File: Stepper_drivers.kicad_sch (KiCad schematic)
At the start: 28 parts, among them J16 Conn_01x04_Socket, J17 Conn_01x02_Socket, J7 Conn_01x04_Socket, J8 Conn_01x02_Socket, U4 LTV-247, U6 AM26LS31CDR

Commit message: New PSU designs + footprints assigned. Changes to board shape to make room for new components. BOM consolidation of supplimentary file
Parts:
- J10: renamed from J8; Digikey Part Number 1818-QT04ADP83V0000G-ND -> 1818-QT02ADP83V0000G-ND; Digikey URL https://www.digikey.com.au/en/products/detail/amphenol-anytek/QT04ADP83V0000G/25618782 -> https://www.digikey.com.au/en/products/detail/amphenol-anytek/QT02ADP83V0000G/25618889
- J7: renamed from J16; Digikey Part Number 1818-QT02ADP83V0000G-ND -> 1818-QT04ADP83V0000G-ND; Digikey URL https://www.digikey.com.au/en/products/detail/amphenol-anytek/QT02ADP83V0000G/25618889 -> https://www.digikey.com.au/en/products/detail/amphenol-anytek/QT04ADP83V0000G/25618782
- J8: renamed from J17; Digikey Part Number 1818-QT04ADP83V0000G-ND -> 1818-QT02ADP83V0000G-ND; Digikey URL https://www.digikey.com.au/en/products/detail/amphenol-anytek/QT04ADP83V0000G/25618782 -> https://www.digikey.com.au/en/products/detail/amphenol-anytek/QT02ADP83V0000G/25618889
- J9: renamed from J7; Digikey Part Number 1818-QT02ADP83V0000G-ND -> 1818-QT04ADP83V0000G-ND; Digikey URL https://www.digikey.com.au/en/products/detail/amphenol-anytek/QT02ADP83V0000G/25618889 -> https://www.digikey.com.au/en/products/detail/amphenol-anytek/QT04ADP83V0000G/25618782
- renumbered C12 to C10, C16 to C11, C32 to C12, C20 to C13, C38 to C14, C11 to C9, R56 to R12, R59 to R13, R62 to R14, R65 to R15, R80 to R16, R83 to R17, R86 to R18, R89 to R19, R92 to R20, R104 to R21, R95 to R22, R105 to R23, R98 to R24, R106 to R25, R101 to R26, R107 to R27, U6 to U5

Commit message: Switched terminal footprints over to a finer pitch. Corrected an issue with component reference values preventing proper use of multi channel rule areas. Component references for 4 channel optos are more straightforward as a result
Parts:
- removed U4: LTV-247, Package_SO:SOP-16_4.4x10.4mm_P1.27mm, symbol Isolator:LTV-247
- added U (x4): LTV-247, Package_SO:SOP-16_4.4x10.4mm_P1.27mm, symbol Isolator:LTV-247
- J: renamed from J8; footprint Amphenol QT:QT02ADP83V0000G -> 691412120002B:691412120002B; Digikey Part Number 1818-QT02ADP83V0000G-ND -> 732-691412120002B-ND; Digikey URL https://www.digikey.com.au/en/products/detail/amphenol-anyt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 -> https://www.digikey.com.au/en/products/detail/w%C3%BCrth-el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
- J: renamed from J7; footprint Amphenol QT:QT04ADP83V0000G -> 691412120004B:691412120004B; Digikey Part Number 1818-QT04ADP83V0000G-ND -> 732-691412120004B-ND; Digikey URL https://www.digikey.com.au/en/products/detail/amphenol-anyt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 -> https://www.digikey.com.au/en/products/detail/w%C3%BCrth-el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
- J10: footprint Amphenol QT:QT02ADP83V0000G -> 691412120002B:691412120002B; Digikey Part Number 1818-QT02ADP83V0000G-ND -> 732-691412120002B-ND; Digikey URL https://www.digikey.com.au/en/products/detail/amphenol-anyt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 -> https://www.digikey.com.au/en/products/detail/w%C3%BCrth-el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
- J9: footprint Amphenol QT:QT04ADP83V0000G -> 691412120004B:691412120004B; Digikey Part Number 1818-QT04ADP83V0000G-ND -> 732-691412120004B-ND; Digikey URL https://www.digikey.com.au/en/products/detail/amphenol-anyt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 -> https://www.digikey.com.au/en/products/detail/w%C3%BCrth-el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
- renumbered U5 to U
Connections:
- net +5VD: now also U.16, U.16, U.16, U.16
- net GNDREF: now also U.2, U.2, U.2, U.2
- net at R12.2: now also U.1
- net at R17.2, U.7 (2A): now also U.15
- net at R13.2: now also U.1
- net at R19.2, U.15 (4A): now also U.15
- net at R16.2, U.1 (1A): now also U.15
- net at R18.2, U.9 (3A): now also U.15
- net at R14.2: now also U.1
- net at R15.2: now also U.1

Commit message: Added 3d Models for new terminal connectors for easy board verification before committing to build
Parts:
- renumbered J to J7, J to J8, U to U4, U to U5
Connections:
- net +5VD: now also U4.10, U4.12, U4.14; no longer U4.16, U4.16, U4.16
- net GNDREF: now also U4.4, U4.6, U4.8; no longer U4.2, U4.2, U4.2
- net at R15.2: now also U4.7; no longer U4.1
- net at R19.2, U5.15 (4A): now also U4.9; no longer U4.15
- net at R13.2: now also U4.3; no longer U4.1
- net at R17.2, U5.7 (2A): now also U4.13; no longer U4.15
- net at R18.2, U5.9 (3A): now also U4.11; no longer U4.15
- net at R14.2: now also U4.5; no longer U4.1

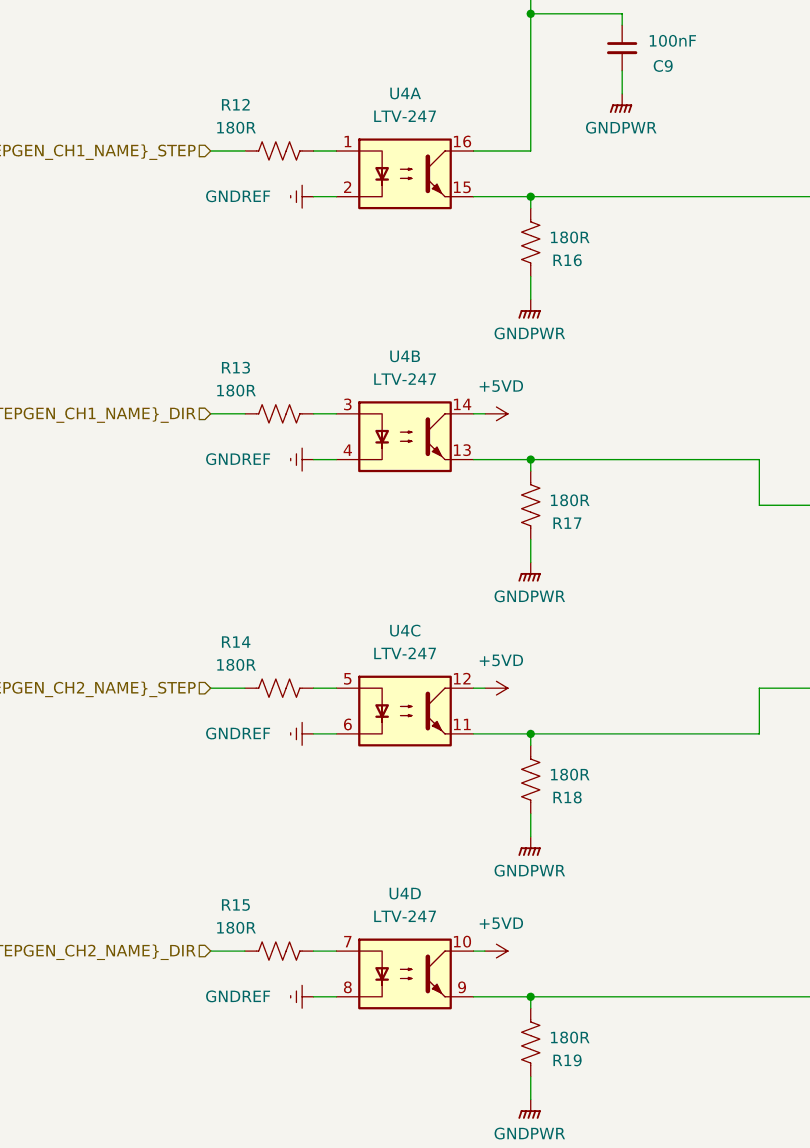
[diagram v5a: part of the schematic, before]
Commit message: Caught some errors with spacing of jumpers, did some BOM consolidation and included BOM. Updates to Gerbers to reflect new changes.
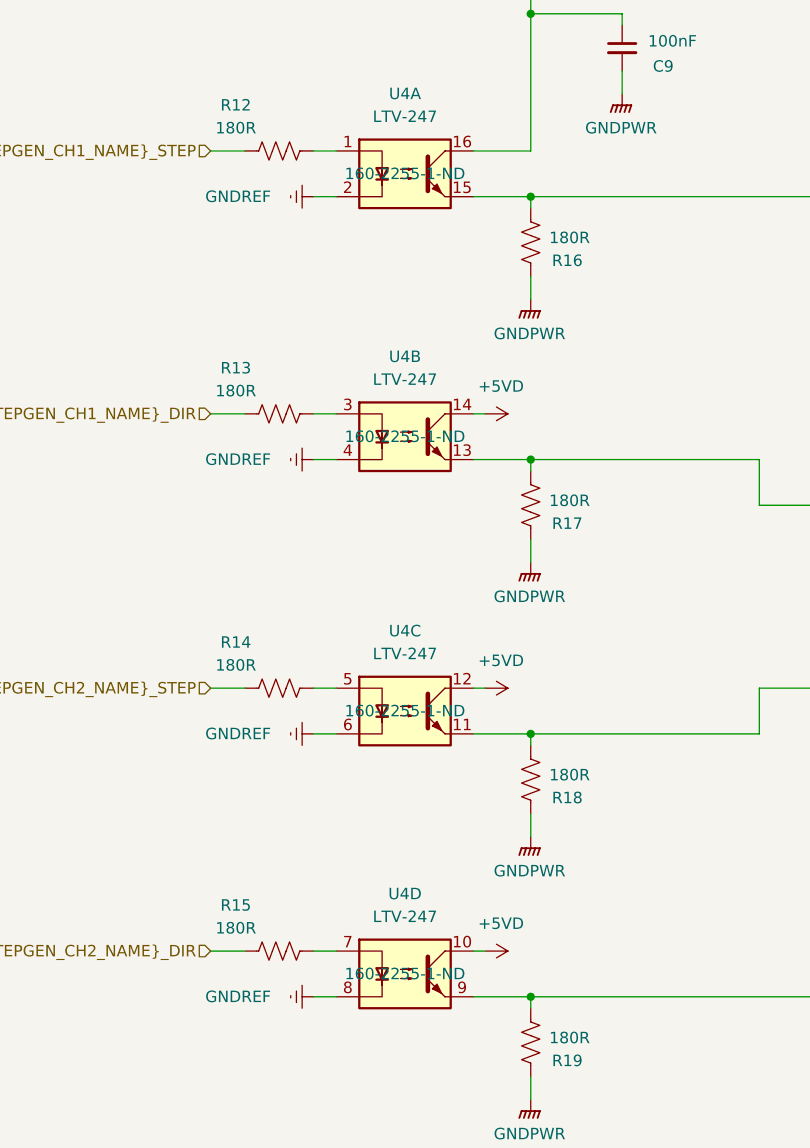
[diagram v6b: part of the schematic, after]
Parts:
- U4: Digikey Part Number (none) -> 160-2255-1-ND
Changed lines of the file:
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@@
 			)
 		)
+		(property "Digikey Part Number" "160-2255-1-ND"
+			(at 50.8 147.32 0)
+			(effects
+				(font
+					(size 1.27 1.27)
+				)
+			)
+		)
 		(pin "14"
 		)
@@
 			)
 		)
+		(property "Digikey Part Number" "160-2255-1-ND"
+			(at 50.8 58.42 0)
+			(effects
+				(font
+					(size 1.27 1.27)
+				)
+			)
+		)
 		(pin "14"
 		)
@@
 			)
 		)
+		(property "Digikey Part Number" "160-2255-1-ND"
+			(at 50.8 118.11 0)
+			(effects
+				(font
+					(size 1.27 1.27)
+				)
+			)
+		)
 		(pin "14"
 		)
@@
 			)
 		)
+		(property "Digikey Part Number" "160-2255-1-ND"
+			(at 50.8 87.63 0)
+			(effects
+				(font
+					(size 1.27 1.27)
+				)
+			)
+		)

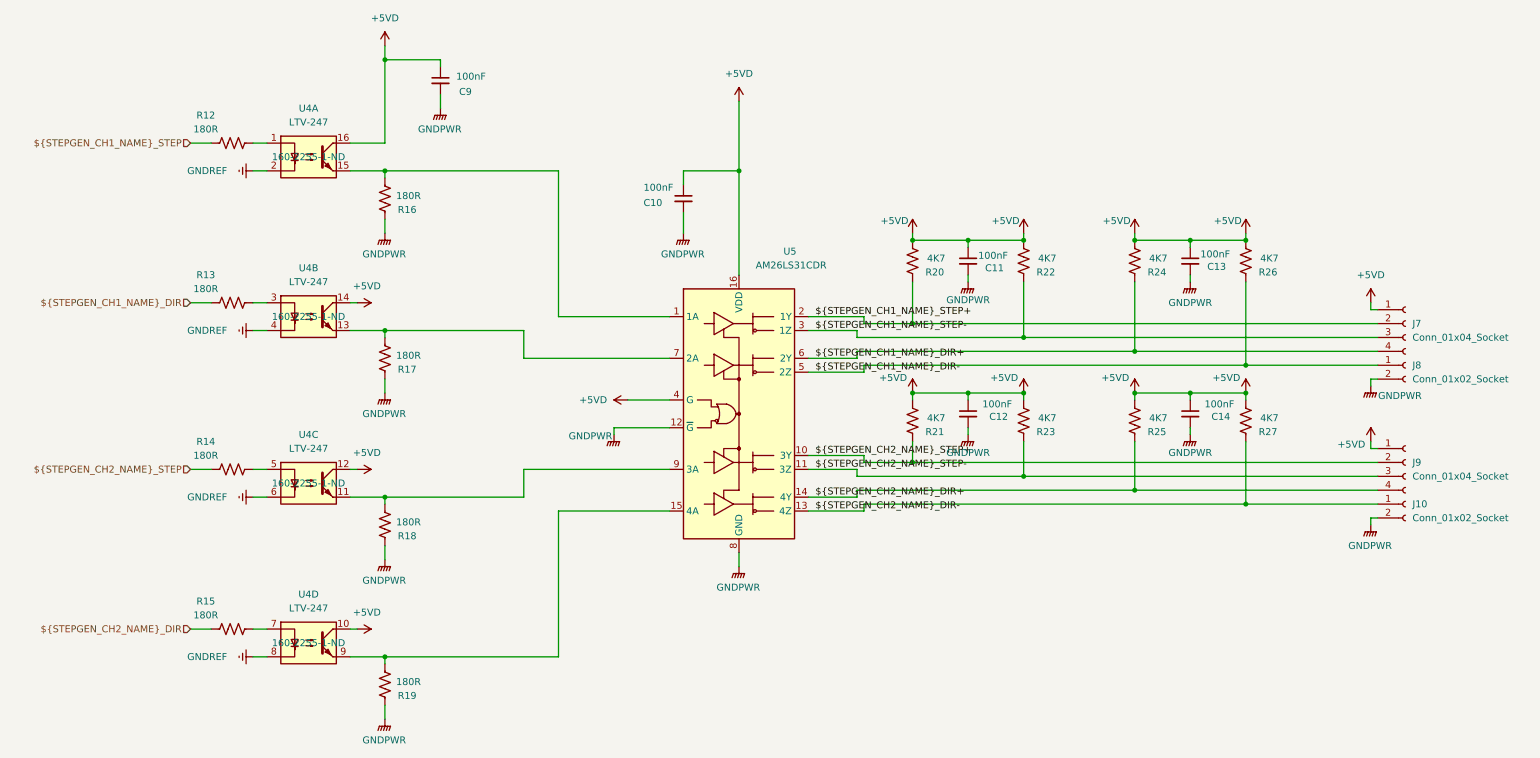
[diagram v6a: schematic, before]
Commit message: Some file changes and output new gerbers + BOM and centroid file for PCBWay Order
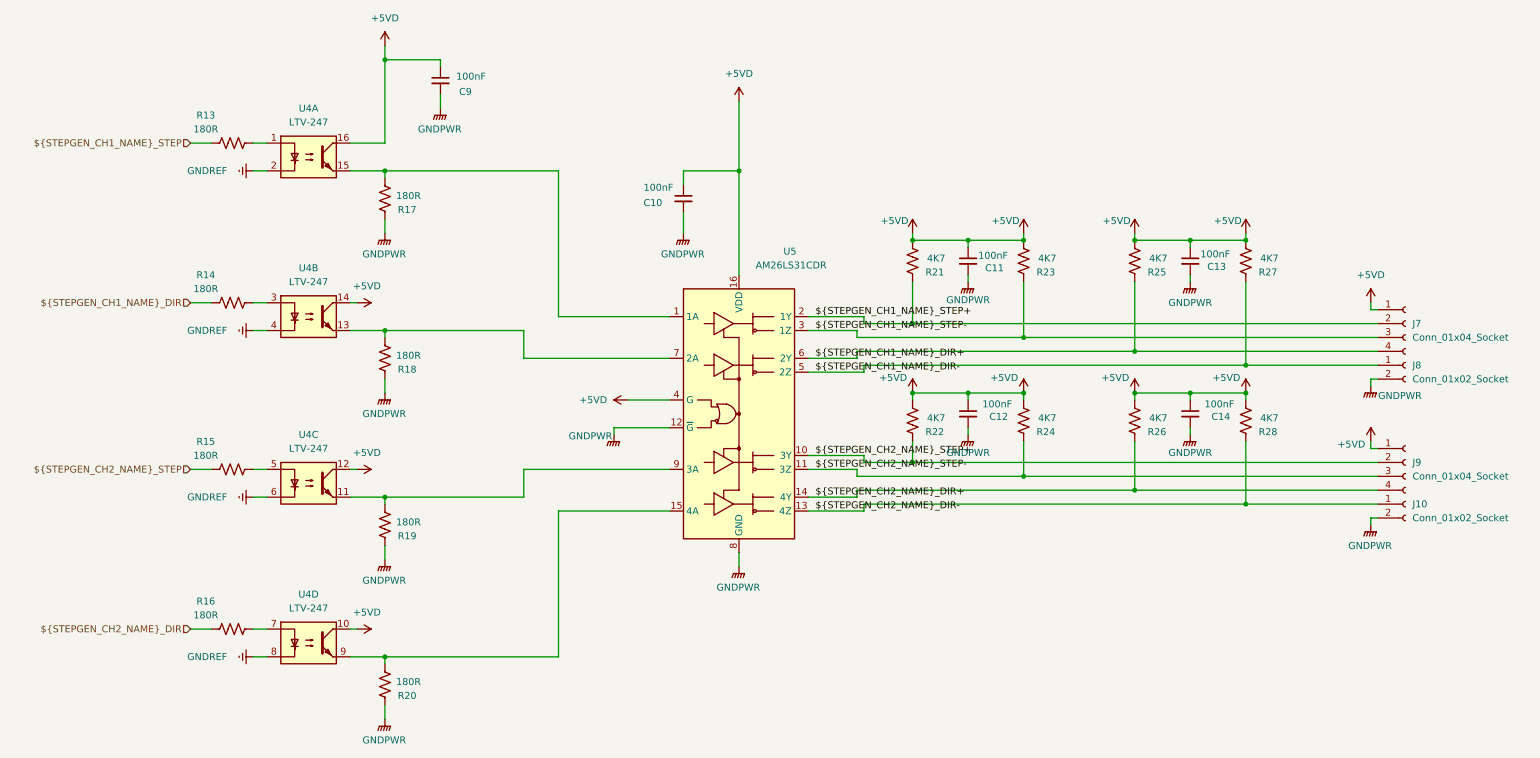
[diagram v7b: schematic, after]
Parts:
- U4: Digikey URL (none) -> https://www.digikey.com.au/en/products/detail/lite-on-inc/l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
- renumbered R12 to R13, R13 to R14, R14 to R15, R15 to R16, R16 to R17, R17 to R18, R18 to R19, R19 to R20, R20 to R21, R21 to R22, R22 to R23, R23 to R24, R24 to R25, R25 to R26, R26 to R27, R27 to R28

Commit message: Updates to readme, working through testing and validation of board. Corrected pull ups on differential stepper outputs. Slight tweak to encoder. Tidied up some traces. Somehow lost the mounting holes and need to remember to put them back
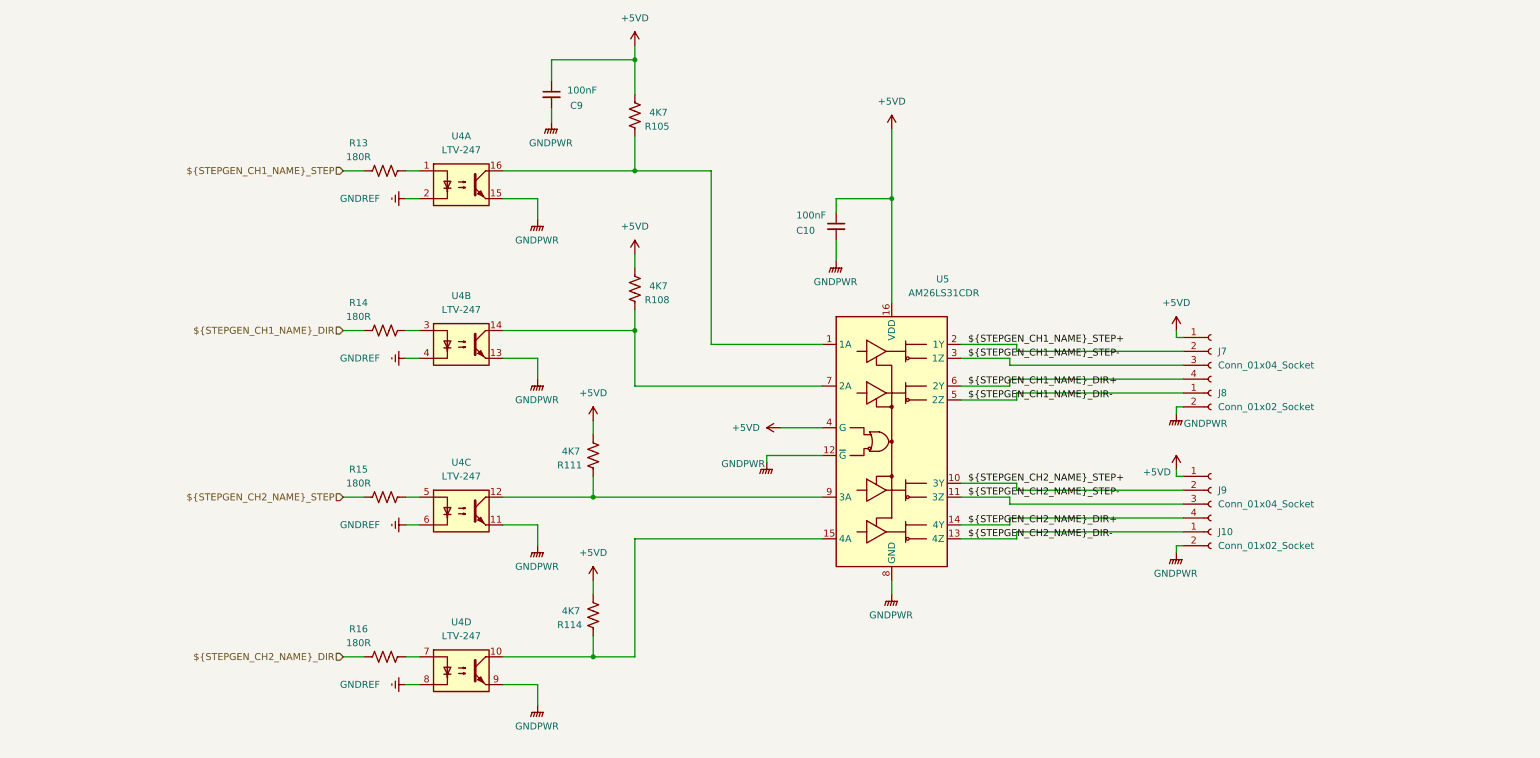
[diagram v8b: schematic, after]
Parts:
- removed C11, C12, C13, C14: 100nF, Capacitor_SMD:C_1206_3216Metric_Pad1.33x1.80mm_HandSolder, symbol Device:C_Small
- removed R17, R18, R19, R20: 180R, Resistor_SMD:R_1206_3216Metric_Pad1.30x1.75mm_HandSolder, symbol Device:R_US
- removed R21, R22, R23, R24, R25, R26, R27, R28: 4K7, Resistor_SMD:R_1206_3216Metric_Pad1.30x1.75mm_HandSolder, symbol Device:R_US
- added R105, R108, R111, R114: 4K7, Resistor_SMD:R_1206_3216Metric_Pad1.30x1.75mm_HandSolder, symbol Device:R_US
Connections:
- net +5VD: now also R105.2, R108.2, R111.2, R114.2; no longer U4.10, U4.12, U4.14, U4.16
- net GNDPWR: now also U4.11, U4.13, U4.15, U4.9
- net at U5.15 (4A): now also U4.10, R114.1; no longer U4.9
- net at U5.7 (2A): now also U4.14, R108.1; no longer U4.13
- net at U5.1 (1A): now also U4.16, R105.1; no longer U4.15
- net at U5.9 (3A): now also U4.12, R111.1; no longer U4.11
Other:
- moved on the sheet: C10, C9, J10, J7, J8, J9, R13, R14, R15, R16, U4A, U4B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
